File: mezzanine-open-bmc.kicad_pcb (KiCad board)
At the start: 2 copper layers, 122 x 54 mm, 42 parts, among them P1 CONN_02X20, P2 CONN_02X20, SW1 PWR, SW2 RST, U1 FT230XS, U4 PCA9306

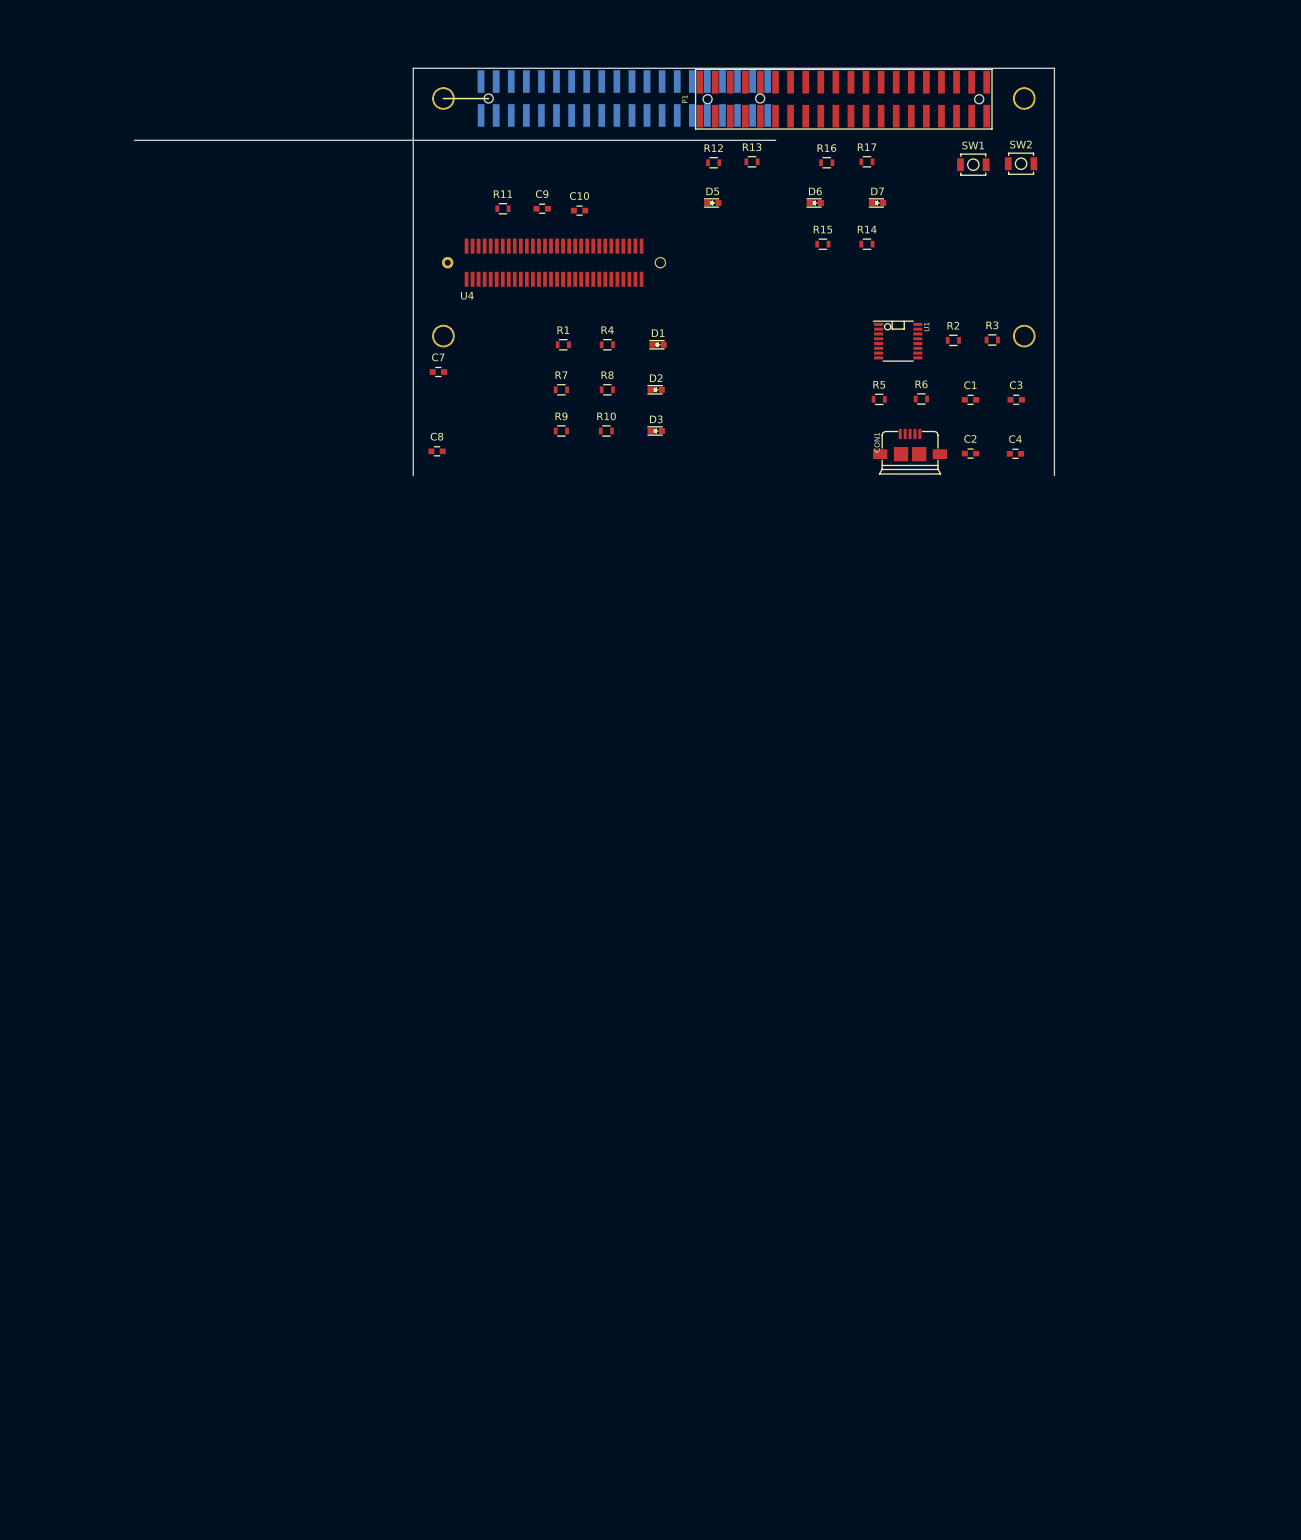
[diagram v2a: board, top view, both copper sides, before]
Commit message: Connect Header Pins
This is a first draft of the connections between the two header pins. This layout
may not be the most efficient therefore is likely to be changed.

Signed-off-by: Sophie Haynes <sophie.haynes@linaro.org>
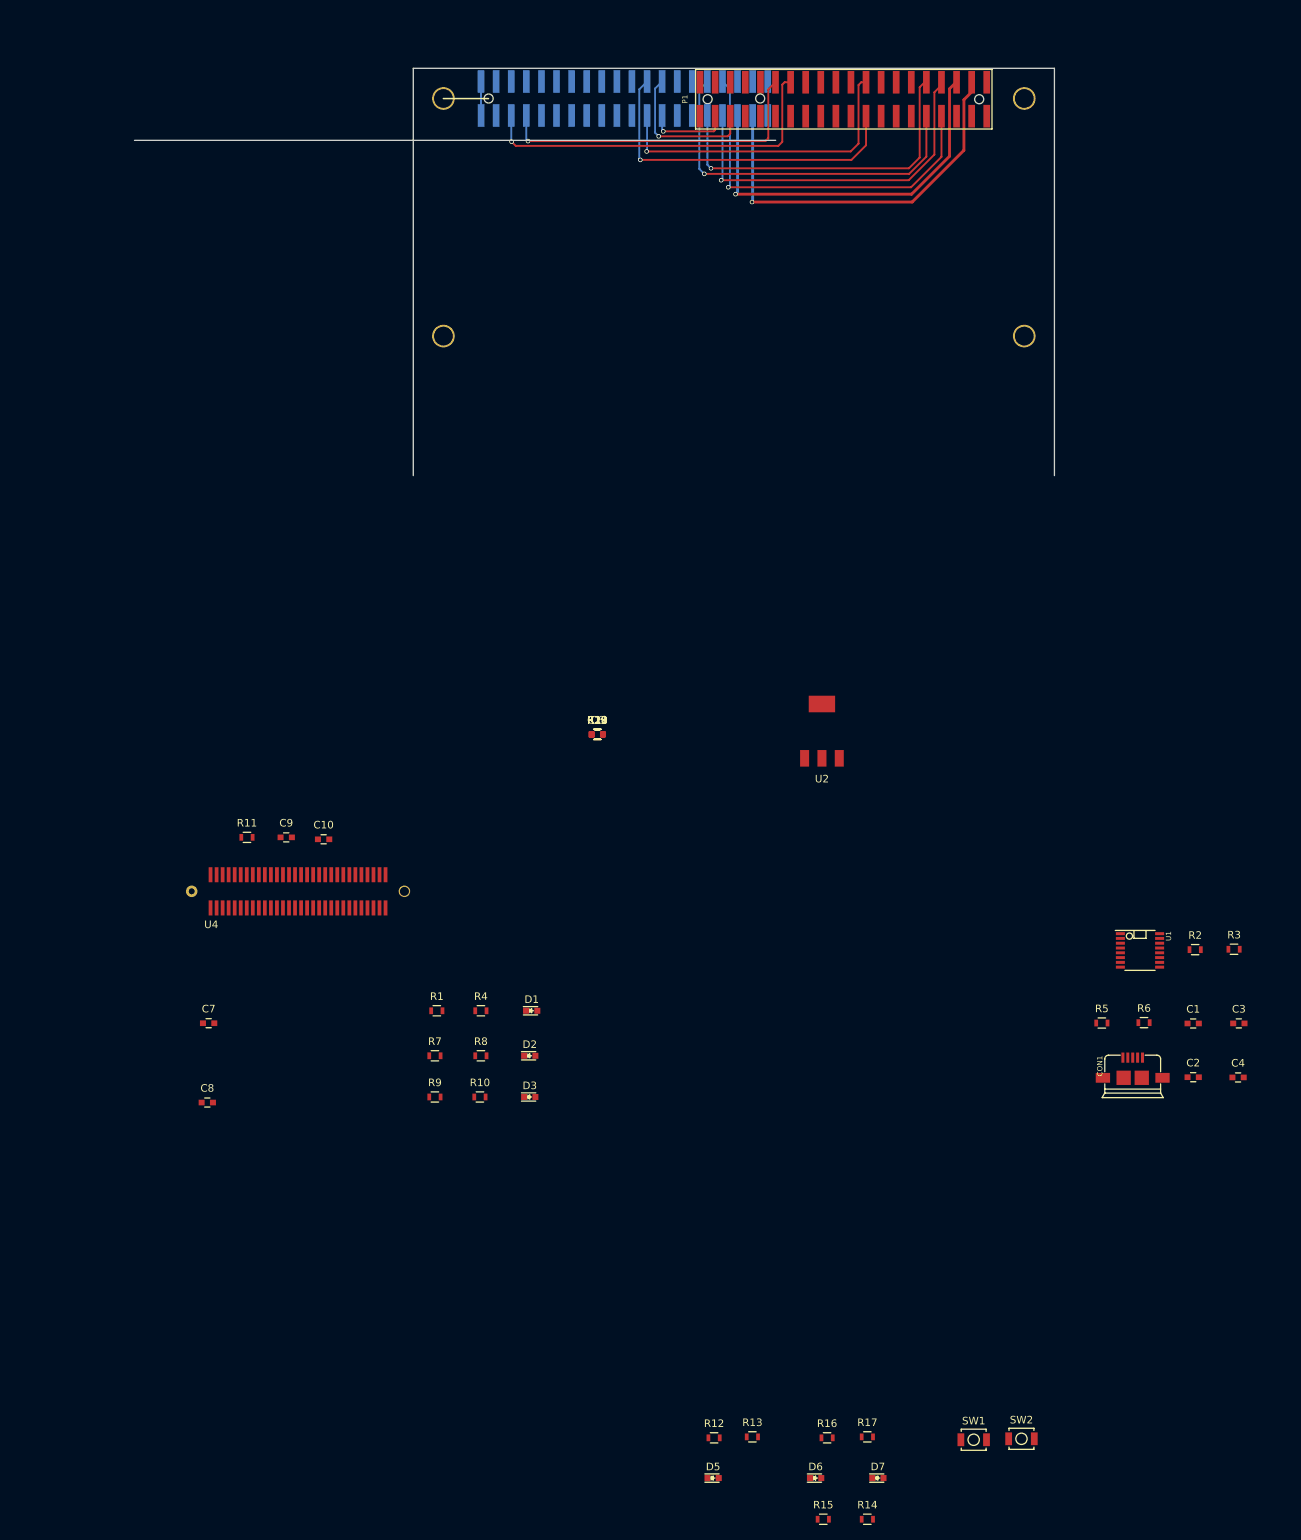
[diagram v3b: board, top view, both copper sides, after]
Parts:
- added C11: 0.1uF, Capacitors_SMD:C_0603, F.Cu at (124.4, 188.3)
- added C6: 0.47u, Capacitors_SMD:C_0603, F.Cu at (124.4, 188.3)
- added R18, R19: 2.2K Ω, Resistors_SMD:R_0603, F.Cu at (124.4, 188.3)
- added R20: 10KΩ, Resistors_SMD:R_0603, F.Cu at (124.4, 188.3)
- added U2: PMIC-CJT1117-3.3(SOT223), 96boards:SOT-223, F.Cu at (154.2, 187.5)
- C3: value C_Small -> 10uF
- C4: value C_Small -> 0.1uF
- C7: value 0.47u -> 33u
- moved R13 169.0 mm to (145.0, 281.4)
- moved R17 169.0 mm to (160.2, 281.4)
- moved D5 169.0 mm to (139.8, 286.9)
- moved D6 169.0 mm to (153.3, 286.9)
- moved D7 169.0 mm to (161.6, 286.9)
- moved R12 169.0 mm to (139.9, 281.6)
- moved R14 169.0 mm to (160.2, 292.4)
- moved R15 169.0 mm to (154.4, 292.4)
- moved R16 169.0 mm to (154.9, 281.6)
- moved SW1 169.0 mm to (174.3, 281.8)
- moved SW2 169.0 mm to (180.6, 281.7)
- moved C7 91.5 mm to (72.9, 226.6)
- moved C8 91.5 mm to (72.7, 237.1)
- moved C9 90.0 mm to (83.2, 202.0)
- moved R11 90.0 mm to (78.0, 202.0)
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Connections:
- C1 pad 2: +3V3 -> GND
- C10 pad 2: +3V3 -> GND
- C2 pad 2: +3V3 -> GND
- C3 pad 2: +3V3 -> GND
- C4 pad 2: +3V3 -> GND
- C7 pad 2: +3V3 -> GND
- C8 pad 2: +3V3 -> GND
- C9 pad 2: +3V3 -> GND
- CON1 pad 5: +3V3 -> GND
- CON1 pad 6: +3V3 -> GND
- CON1 pad 7: +3V3 -> GND
- CON1 pad 8: +3V3 -> GND
- CON1 pad 9: +3V3 -> GND
- D1 pad 1: +3V3 -> GND
- D3 pad 1: +3V3 -> GND
- D5 pad 1: +3V3 -> GND
- D7 pad 1: +3V3 -> GND
- P1 pad 1: +3V3 -> GND
- P1 pad 2: +3V3 -> GND
- P1 pad 39: +3V3 -> GND
- P1 pad 40: +3V3 -> GND
- P2 pad 1: +3V3 -> GND
- P2 pad 2: +3V3 -> GND
- P2 pad 31: GPIO_I_BMC -> GPIO_I
- P2 pad 32: GPIO_J_BMC -> GPIO_J
- P2 pad 33: GPIO_K_BMC -> GPIO_K
- P2 pad 34: GPIO_L_BMC -> GPIO_L
- P2 pad 39: +3V3 -> GND
- P2 pad 40: +3V3 -> GND
- R15 pad 2: +3V3 -> GND
- R8 pad 2: +3V3 -> GND
- SW1 pad 2: +3V3 -> GND
- SW2 pad 2: +3V3 -> GND
- U1 pad 10: +3V3 -> Net-(C11-Pad1)
- U1 pad 11: +3V3 -> Net-(C11-Pad1)
- U1 pad 13: +3V3 -> GND
- U1 pad 5: +3V3 -> GND
- U4 pad 1: +3V3 -> GND
- U4 pad 7: I2C0_SCL_3.3 -> Net-(R18-Pad2)
- U4 pad 8: I2C0_SDA_3.3 -> Net-(R19-Pad2)
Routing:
- net +5V: track 0.00 -> 51.9 mm, vias 0 -> 1
- net +1V8: track 0.00 -> 51.2 mm, vias 0 -> 1
- net GPIO_L: track 0.00 -> 49.9 mm, vias 0 -> 1
- net GPIO_J: track 0.00 -> 48.7 mm, vias 0 -> 1
- net UART0_TX_BMC: track 0.00 -> 48.7 mm, vias 0 -> 1
- net GPIO_K: track 0.00 -> 48.3 mm, vias 0 -> 1
- net GPIO_I: track 0.00 -> 45.9 mm, vias 0 -> 1
- net GPIO_B: track 0.00 -> 45.4 mm, vias 0 -> 1
- net UART0_RX_BMC: track 0.00 -> 43.3 mm, vias 0 -> 1
- net GPIO_A: track 0.00 -> 42.2 mm, vias 0 -> 1
- net GPIO_D_BMC: track 0.00 -> 19.8 mm, vias 0 -> 1
- net GPIO_C_BMC: track 0.00 -> 11.0 mm, vias 0 -> 1
- net GND: track 0.00 -> 4.50 mm

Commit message: [WIP] PCB
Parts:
- moved C1 124.1 mm to (120.7, 134.0)
- moved C2 124.1 mm to (120.7, 141.2)
- moved C3 124.1 mm to (126.8, 134.0)
- moved C4 124.1 mm to (126.7, 141.2)
- moved CON1 124.1 mm to (112.7, 142.7)
- moved R2 124.1 mm to (121.0, 124.3)
- moved R3 124.1 mm to (126.1, 124.2)
- moved R5 124.1 mm to (108.6, 134.0)
- moved R6 124.1 mm to (114.2, 133.9)
- moved U1 124.1 mm to (113.7, 124.4)
- moved D1 107.0 mm to (154.2, 125.1)
- moved D2 107.0 mm to (153.9, 131.1)
- moved D3 107.0 mm to (153.9, 136.6)
- moved R1 107.0 mm to (141.6, 125.1)
- moved R10 107.0 mm to (147.3, 136.6)
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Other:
- board size 122 x 54 mm -> 85 x 54.1 mm
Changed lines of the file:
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@@
     (area 58.5454 87.3 211.671229 295.3245)
     (thickness 1.6)
-    (drawings 12)
+    (drawings 13)
     (tracks 93)
     (zones 0)
@@
   )
   (module Capacitors_SMD:C_0603 (layer F.Cu)
-    (at 203.39578 226.62916)
+    (at 120.71878 134.04616)
     (descr "Capacitor SMD 0603, reflow soldering, AVX (see smccp.pdf)")
     (tags "capacitor 0603")
@@
   )
   (module Capacitors_SMD:C_0603 (layer F.Cu)
-    (at 203.39578 233.75386)
+    (at 120.71878 141.17086)
     (descr "Capacitor SMD 0603, reflow soldering, AVX (see smccp.pdf)")
     (tags "capacitor 0603")
@@
   )
   (module Capacitors_SMD:C_0603 (layer F.Cu)
-    (at 209.4486 226.619)
+    (at 126.7716 134.036)
     (descr "Capacitor SMD 0603, reflow soldering, AVX (see smccp.pdf)")
     (tags "capacitor 0603")
@@
   )
   (module Capacitors_SMD:C_0603 (layer F.Cu)
-    (at 209.347 233.7818)
+    (at 126.67 141.1988)
     (descr "Capacitor SMD 0603, reflow soldering, AVX (see smccp.pdf)")
     (tags "capacitor 0603")
@@
   )
   (module 96boards:USB_MICRO_B_ST-USB-001E (layer F.Cu)
-    (at 195.377 235.3312)
+    (at 112.7 142.7482)
     (descr "USB Micro-B 5-pin SMD connector")
     (tags "USB, Micro-B, connector")
@@
   )
   (module LEDs:LED_0603 (layer F.Cu)
-    (at 115.6972 224.9426)
+    (at 154.1782 125.1206)
     (descr "LED 0603 smd package")
     (tags "LED led 0603 SMD smd SMT smt smdled SMDLED smtled SMTLED")
@@
   )
   (module LEDs:LED_0603 (layer F.Cu)
-    (at 115.4432 230.9116)
+    (at 153.9242 131.0896)
     (descr "LED 0603 smd package")
     (tags "LED led 0603 SMD smd SMT smt smdled SMDLED smtled SMTLED")
@@
   )
   (module LEDs:LED_0603 (layer F.Cu)
-    (at 115.4432 236.3726)
+    (at 153.9242 136.5506)
     (descr "LED 0603 smd package")
     (tags "LED led 0603 SMD smd SMT smt smdled SMDLED smtled SMTLED")
@@
   )
   (module LEDs:LED_0603 (layer F.Cu)
-    (at 139.751 286.8932)
+    (at 127.94 220.9802)
     (descr "LED 0603 smd package")
     (tags "LED led 0603 SMD smd SMT smt smdled SMDLED smtled SMTLED")
@@
   )
   (module LEDs:LED_0603 (layer F.Cu)
-    (at 153.34 286.8932)
+    (at 141.529 220.9802)
     (descr "LED 0603 smd package")
     (tags "LED led 0603 SMD smd SMT smt smdled SMDLED smtled SMTLED")
@@
   )
   (module LEDs:LED_0603 (layer F.Cu)
-    (at 161.595 286.8932)
+    (at 149.784 220.9802)
     (descr "LED 0603 smd package")
     (tags "LED led 0603 SMD smd SMT smt smdled SMDLED smtled SMTLED")
@@
   )
   (module Resistors_SMD:R_0603 (layer F.Cu)
-    (at 103.1242 224.9426)
+    (at 141.6052 125.1206)
     (descr "Resistor SMD 0603, reflow soldering, Vishay (see dcrcw.pdf)")
     (tags "resistor 0603")
@@
   )
   (module Resistors_SMD:R_0603 (layer F.Cu)
-    (at 203.6574 216.84)
+    (at 120.9804 124.257)
     (descr "Resistor SMD 0603, reflow soldering, Vishay (see dcrcw.pdf)")
     (tags "resistor 0603")
@@
   )
   (module Resistors_SMD:R_0603 (layer F.Cu)
-    (at 208.8136 216.7892)
+    (at 126.1366 124.2062)
     (descr "Resistor SMD 0603, reflow soldering, Vishay (see dcrcw.pdf)")
     (tags "resistor 0603")
@@
   )
   (module Resistors_SMD:R_0603 (layer F.Cu)
-    (at 108.9662 224.9426)
+    (at 147.4472 125.1206)
     (descr "Resistor SMD 0603, reflow soldering, Vishay (see dcrcw.pdf)")
     (tags "resistor 0603")
@@
   )
   (module Resistors_SMD:R_0603 (layer F.Cu)
-    (at 191.2876 226.5682)
+    (at 108.6106 133.9852)
     (descr "Resistor SMD 0603, reflow soldering, Vishay (see dcrcw.pdf)")
     (tags "resistor 0603")
@@
   )
   (module Resistors_SMD:R_0603 (layer F.Cu)
-    (at 196.8756 226.5174)
+    (at 114.1986 133.9344)
     (descr "Resistor SMD 0603, reflow soldering, Vishay (see dcrcw.pdf)")
     (tags "resistor 0603")
@@
   )
   (module Resistors_SMD:R_0603 (layer F.Cu)
-    (at 102.8702 230.9116)
+    (at 141.3512 131.0896)
     (descr "Resistor SMD 0603, reflow soldering, Vishay (see dcrcw.pdf)")
     (tags "resistor 0603")
@@
   )
   (module Resistors_SMD:R_0603 (layer F.Cu)
-    (at 108.9662 230.9116)
+    (at 147.4472 131.0896)
     (descr "Resistor SMD 0603, reflow soldering, Vishay (see dcrcw.pdf)")
     (tags "resistor 0603")
@@
   )
   (module Resistors_SMD:R_0603 (layer F.Cu)
-    (at 102.8702 236.3726)
+    (at 141.3512 136.5506)
     (descr "Resistor SMD 0603, reflow soldering, Vishay (see dcrcw.pdf)")
     (tags "resistor 0603")
@@
   )
   (module Resistors_SMD:R_0603 (layer F.Cu)
-    (at 108.8392 236.3726)
+    (at 147.3202 136.5506)
     (descr "Resistor SMD 0603, reflow soldering, Vishay (see dcrcw.pdf)")
     (tags "resistor 0603")
@@
   )
   (module Resistors_SMD:R_0603 (layer F.Cu)
-    (at 139.878 281.5592)
+    (at 128.067 215.6462)
     (descr "Resistor SMD 0603, reflow soldering, Vishay (see dcrcw.pdf)")
     (tags "resistor 0603")
@@
   )
   (module Resistors_SMD:R_0603 (layer F.Cu)
-    (at 144.958 281.4322)
+    (at 133.147 215.5192)
     (descr "Resistor SMD 0603, reflow soldering, Vishay (see dcrcw.pdf)")
     (tags "resistor 0603")
@@
   )
   (module Resistors_SMD:R_0603 (layer F.Cu)
-    (at 160.198 292.3542)
+    (at 148.387 226.4412)
     (descr "Resistor SMD 0603, reflow soldering, Vishay (see dcrcw.pdf)")
     (tags "resistor 0603")
@@
   )
   (module Resistors_SMD:R_0603 (layer F.Cu)
-    (at 154.356 292.3542)
+    (at 142.545 226.4412)
     (descr "Resistor SMD 0603, reflow soldering, Vishay (see dcrcw.pdf)")
     (tags "resistor 0603")
@@
   )
   (module Resistors_SMD:R_0603 (layer F.Cu)
-    (at 154.864 281.5592)
+    (at 143.053 215.6462)
     (descr "Resistor SMD 0603, reflow soldering, Vishay (see dcrcw.pdf)")
     (tags "resistor 0603")
@@
   )
   (module Resistors_SMD:R_0603 (layer F.Cu)
-    (at 160.198 281.4322)
+    (at 148.387 215.5192)
     (descr "Resistor SMD 0603, reflow soldering, Vishay (see dcrcw.pdf)")
     (tags "resistor 0603")
@@
   )
   (module Buttons_Switches_SMD:SW_SPST_B3U-1000P (layer F.Cu)
-    (at 174.295 281.8132)
+    (at 162.484 215.9002)
     (descr "Ultra-small-sized Tactile Switch with High Contact Reliability, Top-actuated Model, without Ground Terminal, without Boss")
     (tags "Tactile Switch")
@@
   )
   (module Buttons_Switches_SMD:SW_SPST_B3U-1000P (layer F.Cu)
-    (at 180.62976 281.6862)
+    (at 168.81876 215.7732)
     (descr "Ultra-small-sized Tactile Switch with High Contact Reliability, Top-actuated Model, without Ground Terminal, without Boss")
     (tags "Tactile Switch")
@@
   )
   (module 96boards:SSOP-16_3.9x4.9mm_Pitch0.635mm_Seeed (layer F.Cu)
-    (at 196.3422 216.9416)
+    (at 113.6652 124.3586)
     (descr "SSOP16: plastic shrink small outline package; 16 leads; body width 3.9 mm; lead pitch 0.635; (see NXP SSOP-TSSOP-VSO-REFLOW.pdf and sot519-1_po.pdf)")
     (tags "SSOP 0.635")
@@
       (net 84 GND))
   )
+  (gr_line (start 100 100) (end 184.999492 100) (angle 90) (layer Edge.Cuts) (width 0.1))
   (gr_line (start 103.9878 104.0132) (end 109.9822 104.0132) (angle 90) (layer F.SilkS) (width 0.2))
   (dimension 18.5 (width 0.3) (layer F.Fab)
@@
     (arrow2b (pts (xy 90 154) (xy 89.413579 152.873496)))
   )
-  (gr_line (start 63.043 109.55) (end 148.042492 109.55) (angle 90) (layer Edge.Cuts) (width 0.1))
+  (gr_line (start 99.9746 154.1016) (end 184.974092 154.1016) (angle 90) (layer Edge.Cuts) (width 0.1))
   (gr_line (start 184.999492 100) (end 184.999492 154) (angle 90) (layer Edge.Cuts) (width 0.1))
   (gr_line (start 100 154) (end 100 100) (angle 90) (layer Edge.Cuts) (width 0.1))
